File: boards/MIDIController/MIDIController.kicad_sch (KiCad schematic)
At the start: 13 parts, among them J1 Ctrl, J4 USB_A, J5 I2S_Data, J6 I2C_Pwr, J7 Raspberry_Pi_2_3, J8 RJ45_Amphenol_RJMG1BD3B8K1ANR, U1 Teensy4.1

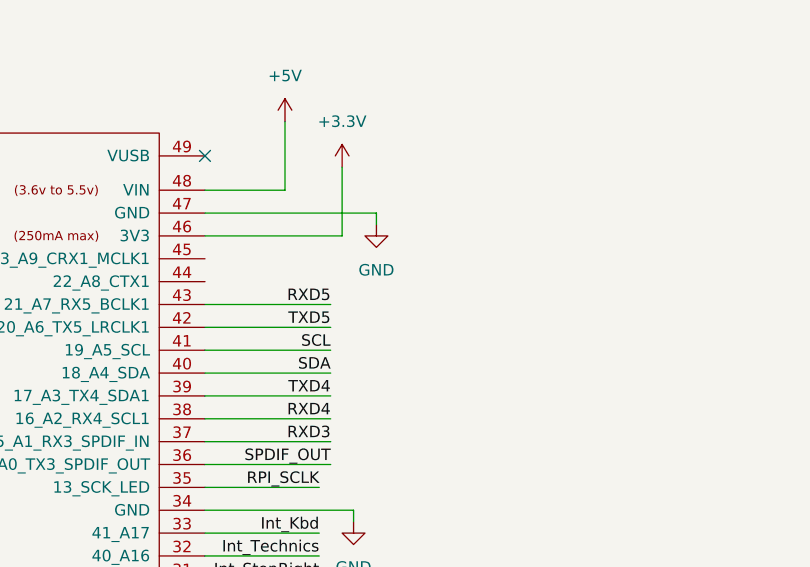
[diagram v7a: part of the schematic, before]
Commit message: Fixed interrupt line to use open collector, added pullups to I2C lines
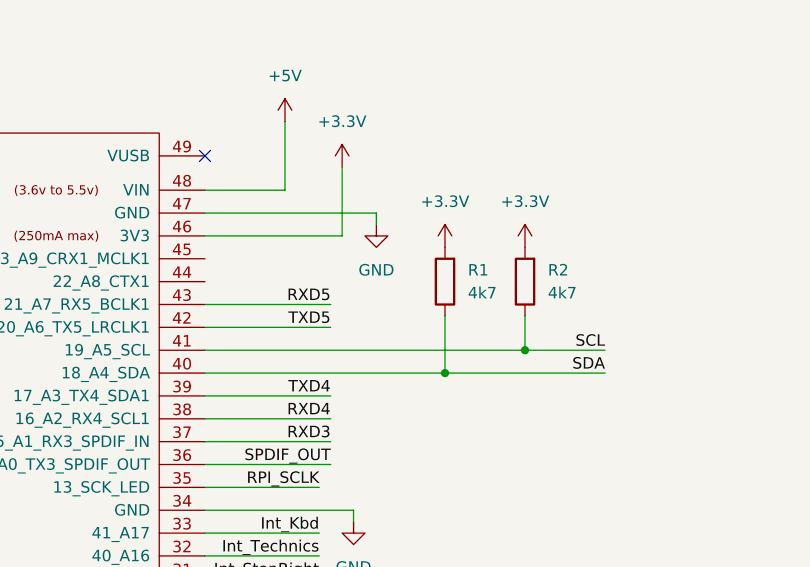
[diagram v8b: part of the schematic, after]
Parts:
- added R1, R2: 4k7, Resistor_THT:R_Axial_DIN0207_L6.3mm_D2.5mm_P10.16mm_Horizontal, symbol Device:R
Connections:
- net +3.3V: now also R1.2, R2.2
- net SCL: now also R2.1
- net SDA: now also R1.1
